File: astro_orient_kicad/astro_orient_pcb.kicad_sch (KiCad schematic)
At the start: 34 parts, among them J1 BME260, J2 SWD_Tag_Connect, J3 USB-C_Receptacle, J4 test_points, SW1 SW_SPST, SW2 SW_Reset, SW3 SW_Boot, U1 STM32F072CBTx, U2 AP2112K-3.3, Y1 osc_crystal

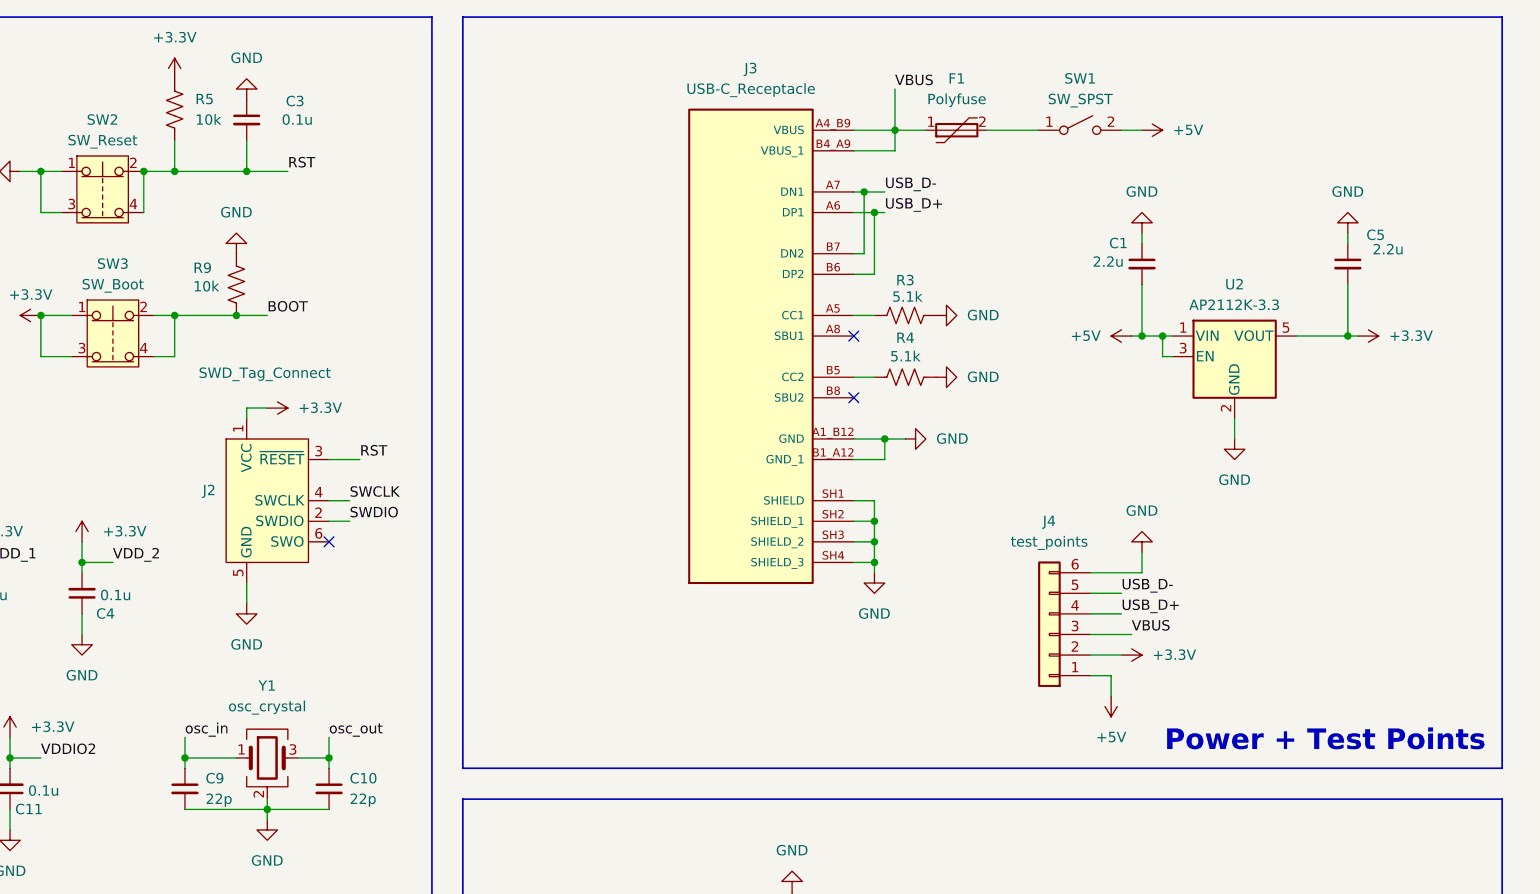
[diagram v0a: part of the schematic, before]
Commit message: Fixed kicad electrical rules errors. schematic should be complete
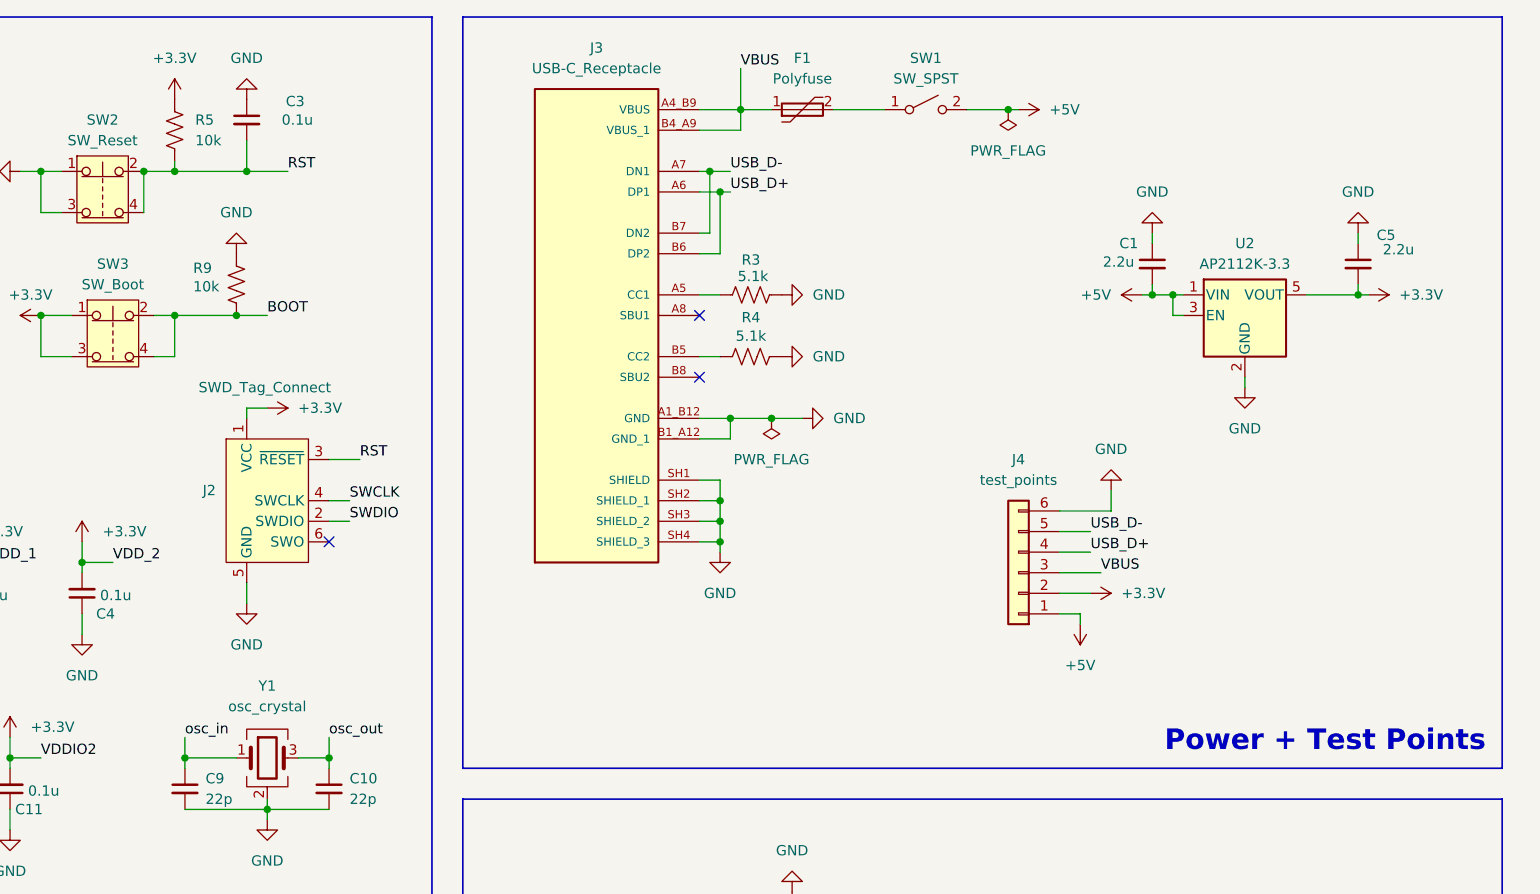
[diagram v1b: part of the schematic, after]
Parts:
- R5, R6, R7, R9: footprint (none) -> imported_footprints:RC0805N_YAG-L
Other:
- moved on the sheet: C1, C5, F1, J3, J4, R3, R4, R5, SW1, U2

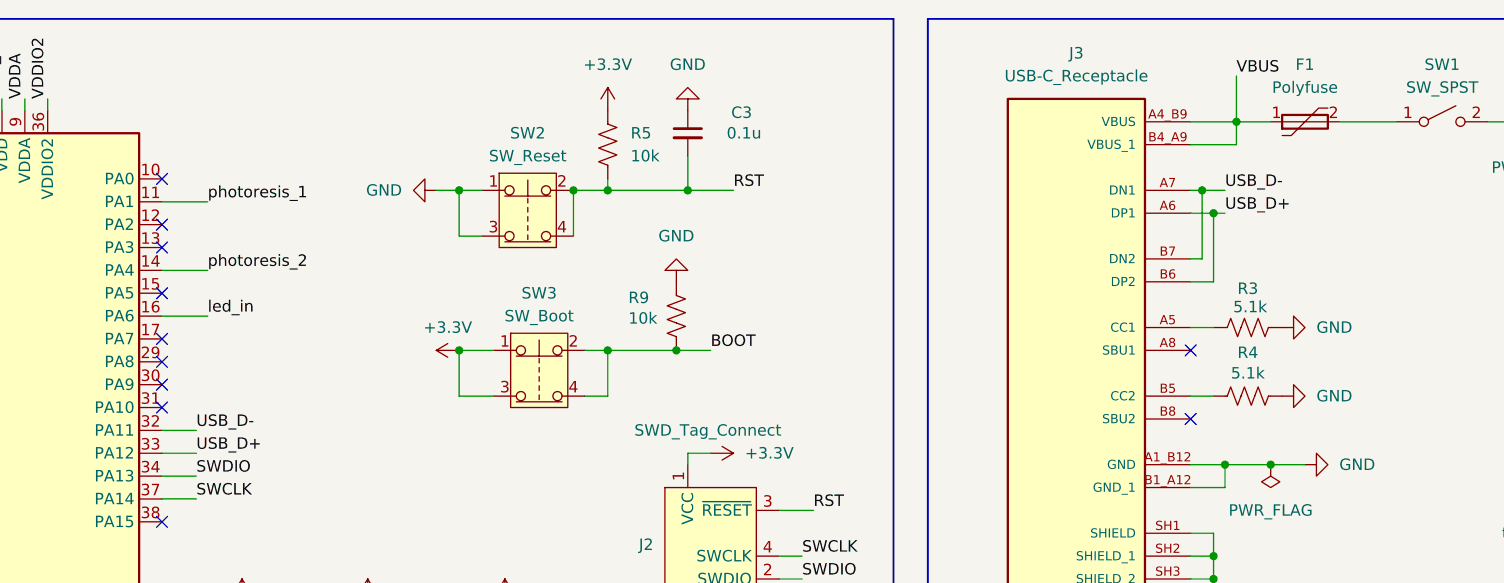
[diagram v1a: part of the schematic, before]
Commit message: updated footprints on PCB
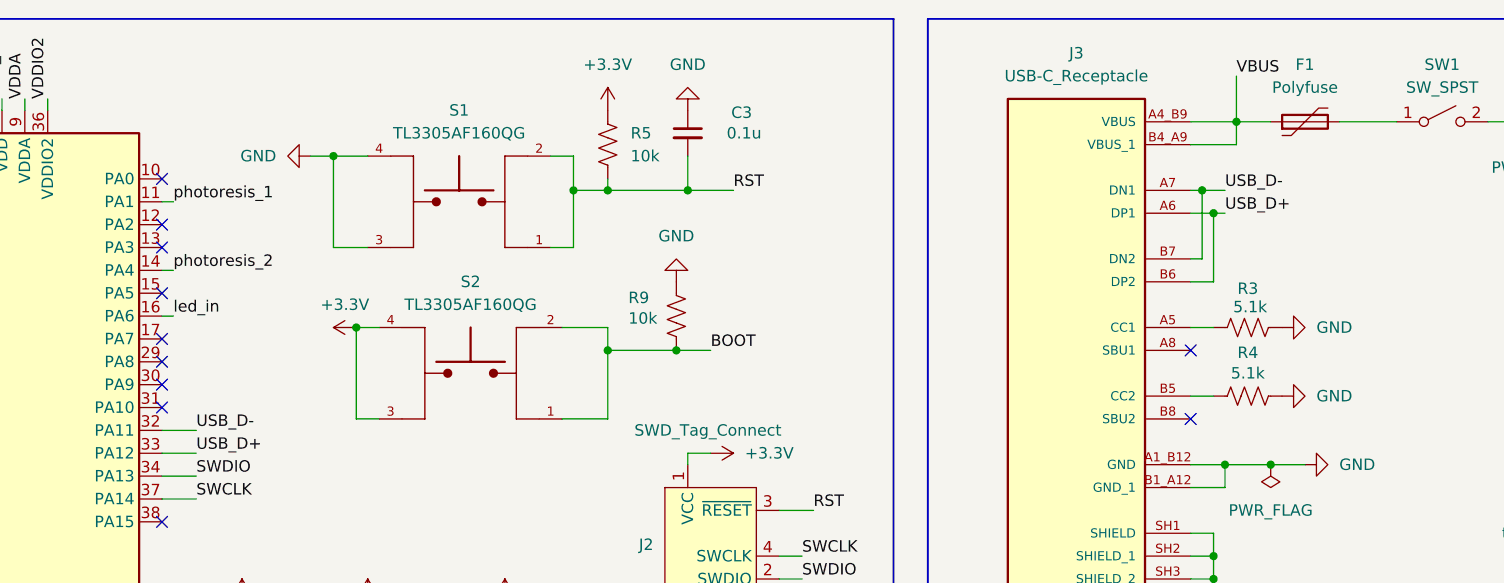
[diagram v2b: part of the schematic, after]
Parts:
- removed SW2: SW_Reset, symbol Switch:SW_Push_Open_Dual
- removed SW3: SW_Boot, symbol Switch:SW_Push_Open_Dual
- added S1, S2: TL3305AF160QG, imported_footprints:SW_TL3305AF160QG, symbol custom_symbols:TL3305AF160QG
- C1, C11, C2, C3, C4, C5, C6, C7, C8: footprint (none) -> Capacitor_SMD:C_0805_2012Metric
- C10, C9: footprint (none) -> Capacitor_SMD:C_0603_1608Metric
- D1: footprint LED_SMD:LED_SK6812MINI_PLCC4_3.5x3.5mm_P1.75mm -> imported_footprints:LED_1655
- D2, D3: footprint LED_SMD:LED_SK6812MINI_PLCC4_3.5x3.5mm_P1.75mm -> Connector_PinHeader_2.54mm:PinHeader_1x04_P2.54mm_Vertical
- F1: footprint (none) -> Fuse:Fuse_1812_4532Metric
- J1: footprint (none) -> Connector_PinHeader_2.54mm:PinHeader_1x07_P2.54mm_Vertical
- J3: footprint UJ20-C-H-G-MSMT-9B-P16-TR:SAMESKY_UJ20-C-H-G-MSMT-9B-P16-TR -> imported_footprints:SAMESKY_UJ20-C-H-G-MSMT-P16-TR
- J4: footprint (none) -> Connector_PinHeader_2.54mm:PinHeader_1x06_P2.54mm_Vertical
- R1, R2: footprint (none) -> imported_footprints:PHODET_PDV-P8103
- R3, R4: footprint (none) -> Resistor_SMD:R_0402_1005Metric
- R8: footprint (none) -> Resistor_SMD:R_2512_6332Metric
- SW1: footprint (none) -> Connector_PinHeader_2.54mm:PinHeader_1x02_P2.54mm_Vertical
- U2: footprint Package_TO_SOT_SMD:SOT-23-5 -> imported_footprints:SOT95P285X140-5N
- Y1: footprint (none) -> Crystal:Crystal_SMD_Abracon_ABM3B-4Pin_5.0x3.2mm
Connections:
- net +3.3V: now also S2.3, S2.4
- net BOOT: now also S2.1, S2.2
- net GND: now also S1.3, S1.4
- net RST: now also S1.1, S1.2

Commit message: updated schematic, partial layout of PCB
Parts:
- added C12, C13: 2.2u, Capacitor_SMD:C_0805_2012Metric, symbol Device:C_Small
- added C14, C15: 0.1u, Capacitor_SMD:C_0805_2012Metric, symbol Device:C_Small
- added R10, R11: 470, Resistor_SMD:R_2512_6332Metric, symbol Device:R_US
- added U3: AP2112K-3.3, imported_footprints:SOT95P285X140-5N, symbol Regulator_Linear:AP2112K-3.3
- C10, C9: footprint Capacitor_SMD:C_0603_1608Metric -> Capacitor_SMD:C_0805_2012Metric
- J4: footprint Connector_PinHeader_2.54mm:PinHeader_1x06_P2.54mm_Vertical -> Connector_PinHeader_2.54mm:PinHeader_1x07_P2.54mm_Vertical; symbol Connector_Generic:Conn_01x06 -> Connector_Generic:Conn_01x07
- R3, R4: footprint Resistor_SMD:R_0402_1005Metric -> Resistor_SMD:R_0805_2012Metric
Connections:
- net +3.3V: now also J4.3 (Pin_3); no longer C11.2, C8.2, J4.2 (Pin_2), R1.1, R2.1, U1.36 (VDDIO2), U1.9 (VDDA)
- net +5V: now also C12.2, C14.2, C15.2, U3.1 (VIN), U3.3 (EN)
- net GND: now also J4.7 (Pin_7), C12.1, C13.1, C14.1, C15.1, U3.2 (GND); no longer J4.6 (Pin_6)
- net USB_D+: now also J4.5 (Pin_5); no longer J4.4 (Pin_4)
- net USB_D-: now also J4.6 (Pin_6); no longer J4.5 (Pin_5)
- net VBUS: now also J4.4 (Pin_4); no longer J4.3 (Pin_3)
- net at D1.4 (DOUT): no longer D2.2 (DIN)
- net at D3.2 (DIN): now also R11.2; no longer D2.4 (DOUT)
- net led_2: now reaches U1.18 (PB0)
- net led_2: now also R10.1
- net led_3: now reaches U1.19 (PB1)
- net led_3: now also R11.1
- net led_in renamed led_1
- new net: D2.2 (DIN), R10.2
- new net +3.3V_Analog: C11.2, C13.2, C8.2, J4.2 (Pin_2), R1.1, R2.1, U1.36 (VDDIO2), U1.9 (VDDA), U3.5 (VOUT)
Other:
- moved on the sheet: C1, C5, C6, D1, D2, R8, U2

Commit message: completed layout of schematic
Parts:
- removed J4: test_points, Connector_PinHeader_2.54mm:PinHeader_1x07_P2.54mm_Vertical, symbol Connector_Generic:Conn_01x07
- added TP1: GND_TP, TestPoint:TestPoint_Pad_D1.0mm, symbol Connector:TestPoint
- added TP2: 5V_TP, TestPoint:TestPoint_Pad_D1.0mm, symbol Connector:TestPoint
- added TP3: 3.3V_TP, TestPoint:TestPoint_Pad_D1.0mm, symbol Connector:TestPoint
- added TP4: 3.3V_A_TP, TestPoint:TestPoint_Pad_D1.0mm, symbol Connector:TestPoint
- added TP7: VBUS_TP, TestPoint:TestPoint_Pad_D1.0mm, symbol Connector:TestPoint
- C13, C5: value 2.2u -> 10u; footprint Capacitor_SMD:C_0805_2012Metric -> Capacitor_SMD:C_1206_3216Metric
- J3: footprint imported_footprints:SAMESKY_UJ20-C-H-G-MSMT-P16-TR -> imported_footprints:SAMESKY_UJ20-C-H-G-SMT-1-P16-TR_Correct
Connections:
- net +3.3V: now also TP3.1
- net +3.3V_Analog: now also TP4.1
- net +5V: now also TP2.1
- net GND: now also TP1.1
- net VBUS: now also TP7.1
- net led_1: now also U1.19 (PB1); no longer U1.16 (PA6)
- net led_3: now also U1.16 (PA6); no longer U1.19 (PB1)
